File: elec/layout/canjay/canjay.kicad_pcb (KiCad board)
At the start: 6 copper layers, 122 x 100 mm, 150 parts, among them U12 10µH ±20%, U18 10kΩ ±1% 62.5mW, U19 10kΩ ±1% 62.5mW, U20 1µF ±10% 25V X5R, U22 1µF ±10% 25V X5R, U23 10kΩ ±1% 62.5mW, U24 10kΩ ±1% 62.5mW, U25 1µF ±10% 25V X5R, U27 1µF ±10% 25V X5R

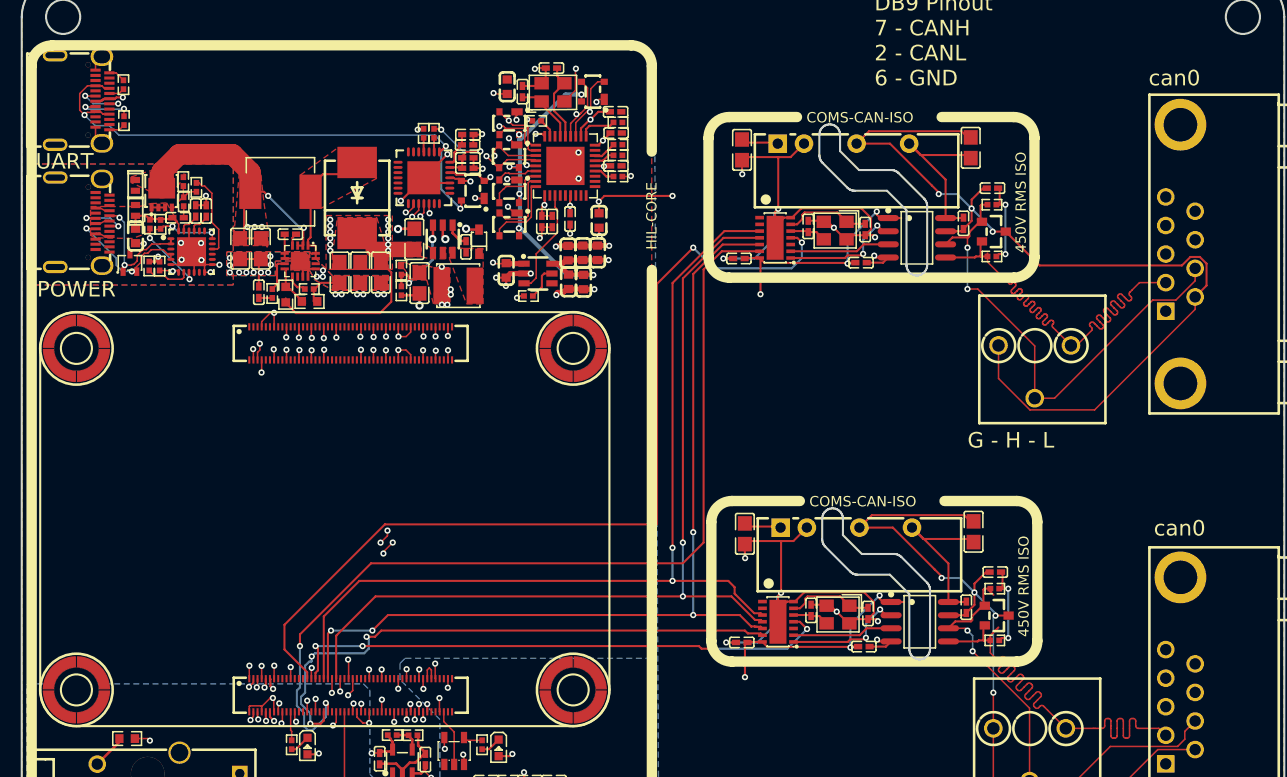
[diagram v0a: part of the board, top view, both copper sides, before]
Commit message: Fix board shapes and CAN termination
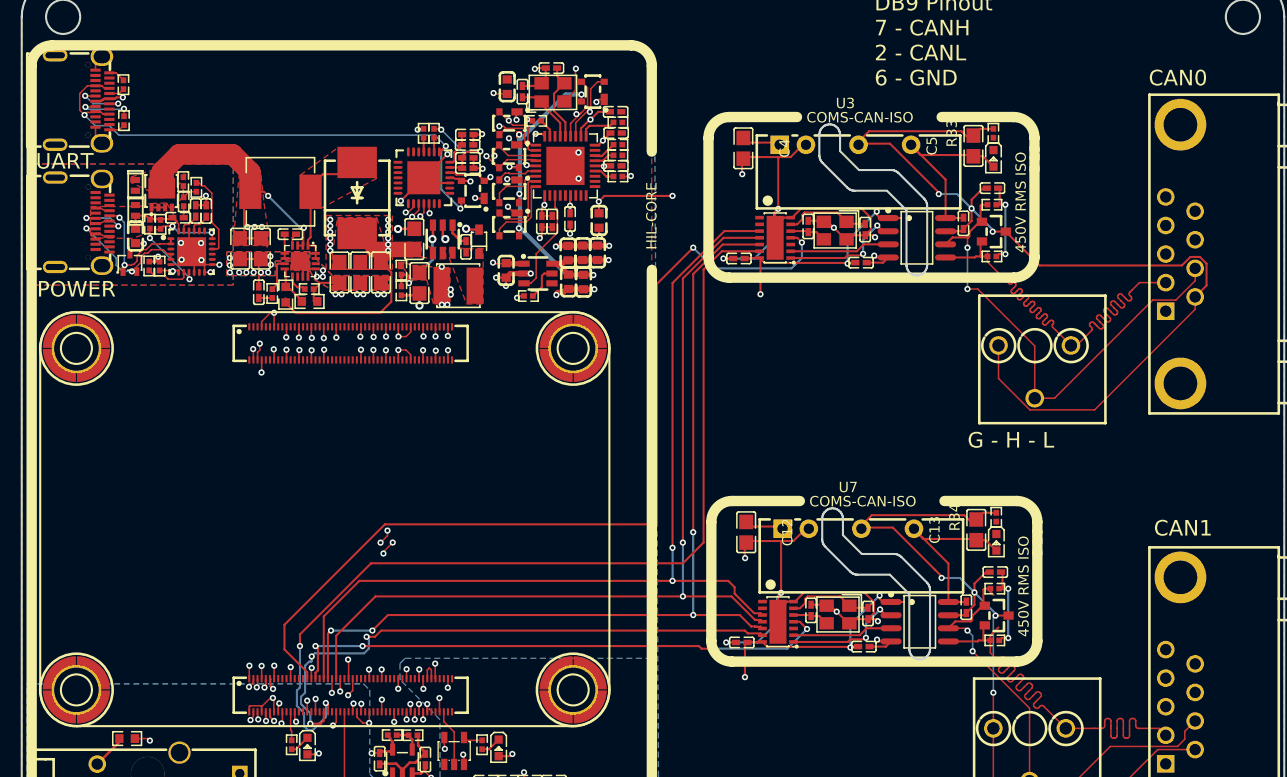
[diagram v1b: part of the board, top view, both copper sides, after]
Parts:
- added D15: , atopile:LED0603-RD-c81ffb, F.Cu at (190.0, 66.4)
- added D16: , atopile:LED0603-RD-c81ffb, F.Cu at (190.3, 103.5)
- added R33: 1kΩ ±1% 62.5mW, atopile:R0402-56259e, F.Cu at (190.0, 64.0)
- added R34: 1kΩ ±1% 62.5mW, atopile:R0402-56259e, F.Cu at (190.3, 101.0)
- C12, C4: value 4.7µF ±10% 25V X5R -> 2.2µF ±10% 25V X7R
- C23, C30, C53: value 4.7µF ±20% 6.3V X5R -> 4.7µF ±20% 10V X5R
- R15: value 560kΩ ±1% 62.5mW -> 510kΩ ±1% 62.5mW
- U14, U15, U16, U17: footprint atopile:SMD_BD5.6-D4.1-12eb58 -> lib:SMD_BD5.6-D4.1-12eb58
- U19: value 10kΩ ±1% 62.5mW -> 18kΩ ±1% 62.5mW
- U24: value 10kΩ ±1% 62.5mW -> 24.9kΩ ±1% 62.5mW
- moved C13 0.32 mm to (188.3, 102.3)
- moved C5 0.32 mm to (188.1, 65.2)
- moved U3 0.22 mm to (175.7, 65.1)
- moved U7 0.22 mm to (176.0, 102.2)
- moved C12 0.20 mm to (166.1, 102.5)
- moved C4 0.20 mm to (165.8, 65.4)
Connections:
- net A6 renamed DP2
- net A7 renamed DN2
- net B5 renamed CC2
- net CC1 renamed A5
- net MDI0plus renamed hil_core.controller-pins[11]
- net MDI2_ renamed hil_core.controller-pins[8]
- net MDI2plus renamed hil_core.controller-pins[10]
- net hil_core.controller-pins[9] renamed MDI0_
- net hil_core.controller.cm5-pins[89] renamed hil_core.controller.cm5-pins[87]-1
- net hil_core.controller.cm5-pins[89]-1 renamed pins[89]
- net hil_core.controller.cm5.hdi_b-pins[9] renamed pins[9]
- net hil_core.ldo_3v3-out renamed hil_core.ldo_3v3-ADJ_NC
- net hil_core.oled.regulator_4v-out renamed hil_core.oled.regulator_4v-ADJ_NC
- net pins[10] renamed hil_core.controller.cm5.hdi_b-pins[10]
- net pins[11] renamed hil_core.controller.cm5.hdi_b-pins[11]
- net pins[87] renamed hil_core.controller.cm5-pins[87]
- net pins[8] renamed hil_core.controller.cm5.hdi_b-pins[8]
- C10 pad 1: xin-2 -> xin
- C13 pad 1: hv -> hv-3
- C16 pad 1: hv -> hv-3
- C18 pad 1: hv-1 -> hv-6
- C19 pad 1: hv-1 -> hv-6
- C29 pad 1: hv-3 -> hv-4
- C30 pad 1: hv-3 -> hv-4
- C42 pad 1: xin -> xin-2
- C45 pad 1: hv-5 -> hv
- C46 pad 1: hv-5 -> hv
- C47 pad 1: hv-5 -> hv
- C48 pad 1: hv-5 -> hv
- C49 pad 1: hv-5 -> hv
- C5 pad 1: hv-2 -> hv-5
- C50 pad 1: hv-4 -> hv-1
- C51 pad 1: hv-4 -> hv-1
- C52 pad 1: hv-6 -> hv-7
- C53 pad 1: hv-6 -> hv-7
- C8 pad 1: hv-2 -> hv-5
- CN1 pad 1: CANL-1 -> CANL
- CN1 pad 2: CANH-1 -> CANH
- CN2 pad 1: CANL -> CANL-1
- CN2 pad 2: CANH -> CANH-1
- CN3 pad 25: hil_core-line-3 -> hil_core-line-6
- CN3 pad 73: hil_core-line-7 -> hil_core-line-8
- CN3 pad 75: hil_core-line -> hil_core-line-5
- CN3 pad 77: hil_core-line-4 -> hil_core-line-10
- CN3 pad 81: line-1 -> line
- CN3 pad 82: line -> line-1
- CN3 pad 86: hil_core-line-5 -> hil_core-line-9
- CN4 pad 98: hil_core-line-8 -> hil_core-line-1
- CN4 pad 99: hil_core-line-10 -> hil_core-line-4
- D1 pad 1: CANH-1 -> CANH
- D1 pad 2: CANL-1 -> CANL
- D10 pad 2: hil_core-line-6 -> hil_core-line-7
- D10 pad 3: hil_core-line-11 -> hil_core-line
- D10 pad 4: hv-5 -> hv
- D11 pad 2: hil_core-line-1 -> hil_core-line-3
- D11 pad 3: hil_core-line-9 -> hil_core-line-11
- D12 pad 1: hil_core.usbpd-line-3 -> hil_core.usbpd-line-2
- D12 pad 2: hil_core.usbpd-line-1 -> hil_core.usbpd-line-3
- D14 pad 1: hv-1 -> hv-6
- D2 pad 1: CANH -> CANH-1
- D2 pad 2: CANL -> CANL-1
- D4 pad 1: hil_core.controller.cm5-cathode-1 -> hil_core.controller.cm5-cathode
- D5 pad 1: hil_core.controller.cm5-cathode -> hil_core.controller.cm5-cathode-1
- D6 pad 2: hil_core-line-1 -> hil_core-line-3
- D6 pad 3: hil_core-line-9 -> hil_core-line-11
- D6 pad 4: hv-5 -> hv
- D7 pad 2: hil_core-line-10 -> hil_core-line-4
- D7 pad 3: hil_core-line-8 -> hil_core-line-1
- D7 pad 4: hv-5 -> hv
- D8 pad 4: hv-5 -> hv
- D9 pad 2: hil_core.usb_hub-line-3 -> hil_core.usb_hub-line
- D9 pad 3: hil_core.usb_hub-line -> hil_core.usb_hub-line-3
- D9 pad 4: hv-5 -> hv
- DSub1 pad 1: can0_db9-net-1 -> can0_db9-net-5
- DSub1 pad 2: CANL-1 -> CANL
- DSub1 pad 3: can0_db9-net -> can0_db9-net-4
- DSub1 pad 4: can0_db9-net-5 -> can0_db9-net
- DSub1 pad 5: can0_db9-net-3 -> can0_db9-net-1
- DSub1 pad 7: CANH-1 -> CANH
- DSub1 pad 8: can0_db9-net-2 -> can0_db9-net-3
- DSub1 pad 9: can0_db9-net-4 -> can0_db9-net-2
- DSub2 pad 1: can1_db9-net-5 -> can1_db9-net-1
- DSub2 pad 2: CANL -> CANL-1
- DSub2 pad 3: can1_db9-net-4 -> can1_db9-net-5
- DSub2 pad 4: can1_db9-net-2 -> can1_db9-net-3
- DSub2 pad 7: CANH -> CANH-1
- DSub2 pad 8: can1_db9-net-1 -> can1_db9-net-4
- DSub2 pad 9: can1_db9-net-3 -> can1_db9-net-2
- L1 pad 1: hv-1 -> hv-6
- OLED1 pad 10: hil_core-line-4 -> hil_core-line-10
- OLED1 pad 14: hv-3 -> hv-4
- OLED1 pad 5: hv-7 -> hv-2
- Q1 pad 5: hv-1 -> hv-6
- Q1 pad 6: hv-1 -> hv-6
- Q1 pad 7: hv-1 -> hv-6
- Q1 pad 8: hv-1 -> hv-6
- Q1 pad 9: hv-1 -> hv-6
- R1 pad 1: CANH-1 -> CANH
- R11 pad 1: hil_core.controller.cm5-cathode-1 -> hil_core.controller.cm5-cathode
- R12 pad 1: hil_core.controller.cm5-cathode -> hil_core.controller.cm5-cathode-1
- R2 pad 2: CANL-1 -> CANL
- R25 pad 2: hv-6 -> hv-7
- R27 pad 1: hil_core.usbpd-line-2 -> hil_core.usbpd-line-1
- R3 pad 1: CANH -> CANH-1
- R30 pad 2: hv-1 -> hv-6
- R4 pad 2: CANL -> CANL-1
- RJ1 pad P1: hil_core.controller.rj45.connector-net -> hil_core.controller.rj45.connector-net-1
- RJ1 pad P10: hil_core.controller.rj45.connector-net-1 -> hil_core.controller.rj45.connector-net
- U1 pad 13: line-1 -> line
- U14 pad 1: hil_core.controller.stud1-net -> GND
- U14 pad 2: hil_core.controller.stud1.footprint.pins[1].net-net -> GND
- U14 pad 3: hil_core.controller.stud1.footprint.pins[2].net-net -> GND
- U14 pad 4: hil_core.controller.stud1.footprint.pins[3].net-net -> GND
- U15 pad 1: hil_core.controller.stud2-net -> GND
- U15 pad 2: hil_core.controller.stud2.footprint.pins[1].net-net -> GND
- U15 pad 3: hil_core.controller.stud2.footprint.pins[2].net-net -> GND
- U15 pad 4: hil_core.controller.stud2.footprint.pins[3].net-net -> GND
- U16 pad 1: hil_core.controller.stud3-net -> GND
- U16 pad 2: hil_core.controller.stud3.footprint.pins[1].net-net -> GND
- U16 pad 3: hil_core.controller.stud3.footprint.pins[2].net-net -> GND
- U16 pad 4: hil_core.controller.stud3.footprint.pins[3].net-net -> GND
- U17 pad 1: hil_core.controller.stud4-net -> GND
- U17 pad 2: hil_core.controller.stud4.footprint.pins[1].net-net -> GND
- U17 pad 3: hil_core.controller.stud4.footprint.pins[2].net-net -> GND
- U17 pad 4: hil_core.controller.stud4.footprint.pins[3].net-net -> GND
- U24 pad 1: hv-7 -> hv-2
- U26 pad 5: hv-7 -> hv-2
- U27 pad 1: hv-7 -> hv-2
- U28 pad 1: hil_core-line-1 -> hil_core-line-3
- U28 pad 2: hil_core-line-9 -> hil_core-line-11
- U28 pad 3: hil_core-line-10 -> hil_core-line-4
- U28 pad 30: hil_core-line-6 -> hil_core-line-7
- U28 pad 31: hil_core-line-11 -> hil_core-line
- U28 pad 33: xin -> xin-2
- U28 pad 4: hil_core-line-8 -> hil_core-line-1
- U28 pad 8: hil_core.usb_hub-line-3 -> hil_core.usb_hub-line
- U28 pad 9: hil_core.usb_hub-line -> hil_core.usb_hub-line-3
- U29 pad 6: hv-5 -> hv
- U3 pad 6: hv-2 -> hv-5
- U30 pad 23: hil_core-line-3 -> hil_core-line-6
- U30 pad 24: hil_core-line-5 -> hil_core-line-9
- U30 pad 25: hil_core-line-7 -> hil_core-line-8
- U30 pad 26: hil_core-line -> hil_core-line-5
- U30 pad 4: hil_core-line-9 -> hil_core-line-11
- U30 pad 5: hil_core-line-1 -> hil_core-line-3
- U30 pad 6: hv-6 -> hv-7
- U30 pad 7: hv-4 -> hv-1
- U31 pad 1: hil_core.usbpd-line-3 -> hil_core.usbpd-line-2
- U31 pad 2: hil_core.usbpd-line-3 -> hil_core.usbpd-line-2
- U31 pad 4: hil_core.usbpd-line-1 -> hil_core.usbpd-line-3
- U31 pad 5: hil_core.usbpd-line-1 -> hil_core.usbpd-line-3
- U31 pad 7: hil_core.usbpd-line-2 -> hil_core.usbpd-line-1
- U32 pad 1: _boardshape.handle-net-1 -> _boardshape.handle-net
- U32 pad 2: _boardshape.handle-net -> _boardshape.handle-net-1
- U4 pad 5: CANL-1 -> CANL
- U4 pad 6: CANH-1 -> CANH
- U4 pad 8: hv-2 -> hv-5
- U5 pad 13: line -> line-1
- U5 pad 6: xin-2 -> xin
- U6 pad 1: xin-2 -> xin
- U7 pad 6: hv -> hv-3
- U8 pad 5: CANL -> CANL-1
- U8 pad 6: CANH -> CANH-1
- U8 pad 8: hv -> hv-3
- U9 pad 2: hv-1 -> hv-6
- U9 pad 3: hv-1 -> hv-6
- USB1 pad A6: hil_core-line-11 -> hil_core-line
- USB1 pad A7: hil_core-line-6 -> hil_core-line-7
- USB1 pad B6: hil_core-line-11 -> hil_core-line
- USB1 pad B7: hil_core-line-6 -> hil_core-line-7
- USB2 pad A5: hil_core.usbpd-line-3 -> hil_core.usbpd-line-2
- USB2 pad B5: hil_core.usbpd-line-1 -> hil_core.usbpd-line-3
- X1 pad 1: xin -> xin-2
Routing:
- net hil_core-line-9: track 15.5 -> 55.0 mm
- net hil_core-line-11: track 54.2 -> 15.5 mm
- net line-1: track 89.5 -> 55.5 mm, vias 2 -> 3
- net line: track 55.5 -> 89.5 mm, vias 3 -> 2
- net hil_core-line-3: track 49.5 -> 16.5 mm, vias 4 -> 2
- net hv-1: track 30.5 -> 3.36 mm, vias 5 -> 0
- net hv: track 16.7 -> 41.6 mm, vias 0 -> 7
- net hv-5: track 41.6 -> 19.0 mm, vias 7 -> 0
- net hil_core-line-1: track 16.5 -> 38.1 mm
- net hv-6: track 10.7 -> 30.5 mm, vias 2 -> 5
- net hv-3: track 4.40 -> 19.0 mm, vias 1 -> 0
- net hil_core-line-8: track 38.1 -> 52.1 mm, vias 2 -> 4
- net hil_core-line-4: track 26.6 -> 38.7 mm, vias 1 -> 2
- net hil_core-line-10: track 38.7 -> 26.6 mm, vias 2 -> 1
- net hil_core.usbpd-line-1: track 13.0 -> 2.17 mm, vias 2 -> 1
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- added copper zone on F.Cu, net hv-6
- removed copper zone on F.Cu, net hv-1
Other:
- board text added: "CAN0"
- board text added: "CAN1"
- board text removed: "can0"

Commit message: drc fixes
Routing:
- net can0.regulator.led-cathode: track 0.00 -> 1.19 mm
- net can1.regulator.led-cathode: track 0.00 -> 1.19 mm
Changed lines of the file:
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@@
 			(remove_unused_layers yes)
 			(keep_end_layers yes)
-			(zone_layer_connections)
+			(zone_layer_connections "In2.Cu")
 			(net 157 "GND")
 		)
@@
 			(remove_unused_layers yes)
 			(keep_end_layers yes)
-			(zone_layer_connections)
+			(zone_layer_connections "In2.Cu")
 			(net 157 "GND")
 		)
@@
 			(remove_unused_layers yes)
 			(keep_end_layers yes)
-			(zone_layer_connections)
+			(zone_layer_connections "In2.Cu")
 			(net 157 "GND")
 		)
@@
 			(remove_unused_layers yes)
 			(keep_end_layers yes)
-			(zone_layer_connections)
+			(zone_layer_connections "In2.Cu")
 			(net 157 "GND")
 		)
@@
 	)
 	(segment
+		(start 190.28 101.48)
+		(end 190.28 102.66)
+		(width 0.15)
+		(layer "F.Cu")
+		(net 311)
+	)
+	(segment
+		(start 190.28 102.66)
+		(end 190.29 102.67)
+		(width 0.15)
+		(layer "F.Cu")
+		(net 311)
+	)
+	(segment
 		(start 182.965 66.05)
 		(end 181.865 64.95)
@@
 	)
 	(segment
+		(start 190.005 64.38)
+		(end 190.005 65.56)
+		(width 0.15)
+		(layer "F.Cu")
+		(net 314)
+	)
+	(segment
+		(start 190.005 65.56)
+		(end 190.015 65.57)
+		(width 0.15)
+		(layer "F.Cu")
+		(net 314)
+	)
+	(segment
 		(start 185.093543 73.42)
 		(end 185.385 73.42)
@@
 		(connect_pads yes
 			(clearance 0)
+		)
+		(min_thickness 0.0254)
+		(filled_areas_thickness no)
+		(fill yes
+			(thermal_gap 0.5)
+			(thermal_bridge_width 0.5)
+			(island_removal_mode 1)
+			(island_area_min 10)
+		)
+		(polygon
+			(pts
+				(xy 136.625011 77.438767) (xy 136.775011 77.438767) (xy 136.994247 76.903058) (xy 136.700011 76.843531)
+				(xy 136.405775 76.903058)
+			)
+		)
+	)
+	(zone
+		(net 261)
+		(net_name "POWER_5V")
+		(layer "F.Cu")
+		(name "$teardrop_padvia$")
+		(hatch full 0.1)
+		(priority 30000)
+		(attr
+			(teardrop
+				(type padvia)
+			)
+		)
+		(connect_pads yes
+			(clearance 0)

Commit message: Build everything with ordered params to fix frozen builds
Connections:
- net A10 renamed hil_core.usbpd.usb_connector-A10
- net A11 renamed hil_core.usbpd.usb_connector-A11
- net A5 renamed CC1
- net B2 renamed hil_core.usbpd.usb_connector-B2
- net B3 renamed hil_core.usbpd.usb_connector-B3
- net B8 renamed hil_core.usbpd.usb_connector-B8
- net CC2 renamed B5
- net DN2 renamed DN1
- net DP2 renamed DP1
- net MDI0_ renamed hil_core.controller-pins[9]
- net MDI1plus renamed hil_core.controller-pins[3]
- net SBU2 renamed hil_core.usb_connector.connector-B8
- net SSRXN2 renamed hil_core.usb_connector.connector-A10
- net SSRXP2 renamed hil_core.usb_connector.connector-A11
- net SSTXN2 renamed hil_core.usb_connector.connector-B3
- net SSTXP2 renamed hil_core.usb_connector.connector-B2
- net hil_core.controller-pins[10] renamed MDI2plus
- net hil_core.controller-pins[11] renamed MDI0plus
- net hil_core.controller-pins[8] renamed MDI2_
- net hil_core.controller.cm5-pins[87] renamed pins[87]
- net hil_core.controller.cm5-pins[87]-1 renamed hil_core.controller.cm5-pins[89]
- net hil_core.controller.cm5.hdi_b-pins[10] renamed pins[10]
- net hil_core.controller.cm5.hdi_b-pins[11] renamed pins[11]
- net hil_core.controller.cm5.hdi_b-pins[8] renamed pins[8]
- net hil_core.usb_connector.connector-A2 renamed hil_core.usb_connector.connector-SSTXP1
- net hil_core.usb_connector.connector-A3 renamed SSTXN1
- net hil_core.usb_connector.connector-A8 renamed SBU1
- net hil_core.usb_connector.connector-B10 renamed SSRXN1
- net hil_core.usb_connector.connector-B11 renamed SSRXP1
- net hil_core.usbpd.usb_connector-A2 renamed hil_core.usbpd.usb_connector-SSTXP1
- net hil_core.usbpd.usb_connector-A3 renamed A3
- net hil_core.usbpd.usb_connector-A8 renamed A8
- net hil_core.usbpd.usb_connector-B10 renamed B10
- net hil_core.usbpd.usb_connector-B11 renamed B11
- net pins[3] renamed hil_core.controller.cm5.hdi_b-pins[3]
- net pins[4] renamed MDI3_
- net pins[89] renamed hil_core.controller.cm5-pins[89]-1
- net pins[9] renamed hil_core.controller.cm5.hdi_b-pins[9]
- C10 pad 1: xin -> xin-2
- C13 pad 1: hv-3 -> hv-4
- C13 pad 2: gnd-1 -> gnd
- C14 pad 2: gnd-1 -> gnd
- C16 pad 1: hv-3 -> hv-4
- C16 pad 2: gnd-1 -> gnd
- C29 pad 1: hv-4 -> hv
- C3 pad 1: xout-1 -> xout
- C30 pad 1: hv-4 -> hv
- C42 pad 1: xin-2 -> xin
- C43 pad 1: xout -> xout-1
- C45 pad 1: hv -> hv-3
- C46 pad 1: hv -> hv-3
- C47 pad 1: hv -> hv-3
- C48 pad 1: hv -> hv-3
- C49 pad 1: hv -> hv-3
- C5 pad 2: gnd -> gnd-1
- C55 pad 2: hil_core.usbpd.pd_controller-hv-1 -> hil_core.usbpd.pd_controller-hv
- C56 pad 2: hil_core.usbpd.pd_controller-hv -> hil_core.usbpd.pd_controller-hv-1
- C6 pad 2: gnd -> gnd-1
- C8 pad 2: gnd -> gnd-1
- CN1 pad 1: CANL -> CANL-1
- CN1 pad 3: gnd -> gnd-1
- CN2 pad 1: CANL-1 -> CANL
- CN2 pad 3: gnd-1 -> gnd
- CN3 pad 23: hil_core-line-2 -> hil_core-line-1
- CN3 pad 24: hil_core.controller.cm5-pins[47] -> hil_core.controller.cm5-pins[47]-1
- CN3 pad 25: hil_core-line-6 -> hil_core-line-8
- CN3 pad 27: hil_core.controller.cm5-pins[53]-1 -> hil_core.controller.cm5-pins[53]
- CN3 pad 73: hil_core-line-8 -> hil_core-line-11
- CN3 pad 75: hil_core-line-5 -> hil_core-line-9
- CN3 pad 76: hil_core.controller.cm5-pins[48]-1 -> hil_core.controller.cm5-pins[48]
- CN3 pad 77: hil_core-line-10 -> hil_core-line-3
- CN3 pad 81: line -> line-1
- CN3 pad 82: line-1 -> line
- CN3 pad 86: hil_core-line-9 -> hil_core-line-5
- CN4 pad 24: hil_core.controller.cm5-pins[47]-1 -> hil_core.controller.cm5-pins[47]
- CN4 pad 27: hil_core.controller.cm5-pins[53] -> hil_core.controller.cm5-pins[53]-1
- CN4 pad 76: hil_core.controller.cm5-pins[48] -> hil_core.controller.cm5-pins[48]-1
- CN4 pad 98: hil_core-line-1 -> hil_core-line-2
- CN4 pad 99: hil_core-line-4 -> hil_core-line-10
- D1 pad 2: CANL -> CANL-1
- D1 pad 3: gnd -> gnd-1
- D10 pad 2: hil_core-line-7 -> hil_core-line-6
- D10 pad 3: hil_core-line -> hil_core-line-7
- D10 pad 4: hv -> hv-3
- D11 pad 2: hil_core-line-3 -> hil_core-line-4
- D11 pad 3: hil_core-line-11 -> hil_core-line
- D12 pad 1: hil_core.usbpd-line-2 -> hil_core.usbpd-line-3
- D12 pad 2: hil_core.usbpd-line-3 -> hil_core.usbpd-line-1
- D16 pad 2: hv-3 -> hv-4
- D2 pad 2: CANL-1 -> CANL
- D2 pad 3: gnd-1 -> gnd
- D6 pad 2: hil_core-line-3 -> hil_core-line-4
- D6 pad 3: hil_core-line-11 -> hil_core-line
- D6 pad 4: hv -> hv-3
- D7 pad 2: hil_core-line-4 -> hil_core-line-10
- D7 pad 3: hil_core-line-1 -> hil_core-line-2
- D7 pad 4: hv -> hv-3
- D8 pad 2: hil_core.usb_hub-line-1 -> hil_core.usb_hub-line-3
- D8 pad 3: hil_core.usb_hub-line-2 -> hil_core.usb_hub-line-1
- D8 pad 4: hv -> hv-3
- D9 pad 3: hil_core.usb_hub-line-3 -> hil_core.usb_hub-line-2
- D9 pad 4: hv -> hv-3
- DSub1 pad 1: can0_db9-net-5 -> can0_db9-net-1
- DSub1 pad 2: CANL -> CANL-1
- DSub1 pad 3: can0_db9-net-4 -> can0_db9-net
- DSub1 pad 4: can0_db9-net -> can0_db9-net-5
- DSub1 pad 5: can0_db9-net-1 -> can0_db9-net-4
- DSub1 pad 6: gnd -> gnd-1
- DSub1 pad 8: can0_db9-net-3 -> can0_db9-net-2
- DSub1 pad 9: can0_db9-net-2 -> can0_db9-net-3
- DSub2 pad 1: can1_db9-net-1 -> can1_db9-net
- DSub2 pad 2: CANL-1 -> CANL
- DSub2 pad 3: can1_db9-net-5 -> can1_db9-net-4
- DSub2 pad 4: can1_db9-net-3 -> can1_db9-net-2
- DSub2 pad 5: can1_db9-net -> can1_db9-net-3
- DSub2 pad 6: gnd-1 -> gnd
- DSub2 pad 8: can1_db9-net-4 -> can1_db9-net-1
- DSub2 pad 9: can1_db9-net-2 -> can1_db9-net-5
- OLED1 pad 10: hil_core-line-10 -> hil_core-line-3
- OLED1 pad 11: hil_core-line-2 -> hil_core-line-1
- OLED1 pad 14: hv-4 -> hv
- R2 pad 2: CANL -> CANL-1
- R27 pad 1: hil_core.usbpd-line-1 -> hil_core.usbpd-line-2
- R33 pad 2: gnd -> gnd-1
- R34 pad 2: gnd-1 -> gnd
- R4 pad 2: CANL-1 -> CANL
- U1 pad 13: line -> line-1
- U1 pad 5: xout-1 -> xout
- U2 pad 3: xout-1 -> xout
- U28 pad 1: hil_core-line-3 -> hil_core-line-4
- U28 pad 2: hil_core-line-11 -> hil_core-line
- U28 pad 3: hil_core-line-4 -> hil_core-line-10
- U28 pad 30: hil_core-line-7 -> hil_core-line-6
- U28 pad 31: hil_core-line -> hil_core-line-7
- U28 pad 32: xout -> xout-1
- U28 pad 33: xin-2 -> xin
- U28 pad 4: hil_core-line-1 -> hil_core-line-2
- U28 pad 6: hil_core.usb_hub-line-1 -> hil_core.usb_hub-line-3
- U28 pad 7: hil_core.usb_hub-line-2 -> hil_core.usb_hub-line-1
- U28 pad 9: hil_core.usb_hub-line-3 -> hil_core.usb_hub-line-2
- U29 pad 6: hv -> hv-3
- U3 pad 4: gnd -> gnd-1
- U30 pad 23: hil_core-line-6 -> hil_core-line-8
- U30 pad 24: hil_core-line-9 -> hil_core-line-5
- U30 pad 25: hil_core-line-8 -> hil_core-line-11
- U30 pad 26: hil_core-line-5 -> hil_core-line-9
- U30 pad 4: hil_core-line-11 -> hil_core-line
- U30 pad 5: hil_core-line-3 -> hil_core-line-4
- U31 pad 1: hil_core.usbpd-line-2 -> hil_core.usbpd-line-3
- U31 pad 2: hil_core.usbpd-line-2 -> hil_core.usbpd-line-3
- U31 pad 21: hil_core.usbpd.pd_controller-hv-1 -> hil_core.usbpd.pd_controller-hv
- U31 pad 23: hil_core.usbpd.pd_controller-hv -> hil_core.usbpd.pd_controller-hv-1
- U31 pad 4: hil_core.usbpd-line-3 -> hil_core.usbpd-line-1
- U31 pad 5: hil_core.usbpd-line-3 -> hil_core.usbpd-line-1
- U31 pad 7: hil_core.usbpd-line-1 -> hil_core.usbpd-line-2
- U32 pad 1: _boardshape.handle-net -> _boardshape.handle-net-1
- U32 pad 2: _boardshape.handle-net-1 -> _boardshape.handle-net
- U4 pad 5: CANL -> CANL-1
- U4 pad 7: gnd -> gnd-1
- U5 pad 13: line-1 -> line
- U5 pad 6: xin -> xin-2
- U6 pad 1: xin -> xin-2
- U7 pad 4: gnd-1 -> gnd
- U7 pad 6: hv-3 -> hv-4
- U8 pad 5: CANL-1 -> CANL
- U8 pad 7: gnd-1 -> gnd
- U8 pad 8: hv-3 -> hv-4
- USB1 pad A6: hil_core-line -> hil_core-line-7
- USB1 pad A7: hil_core-line-7 -> hil_core-line-6
- USB1 pad B6: hil_core-line -> hil_core-line-7
- USB1 pad B7: hil_core-line-7 -> hil_core-line-6
- USB2 pad A5: hil_core.usbpd-line-2 -> hil_core.usbpd-line-3
- USB2 pad B5: hil_core.usbpd-line-3 -> hil_core.usbpd-line-1
- X1 pad 1: xin-2 -> xin
- X1 pad 3: xout -> xout-1
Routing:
- net hil_core-line: track 54.2 -> 15.5 mm
- net hv: track 41.6 -> 4.40 mm, vias 7 -> 1
- net hil_core-line-11: track 15.5 -> 52.1 mm, vias 2 -> 4
- net line-1: track 55.5 -> 89.5 mm, vias 3 -> 2
- net line: track 89.5 -> 55.5 mm, vias 2 -> 3
- net hv-3: track 19.0 -> 41.6 mm, vias 0 -> 7
- net hil_core-line-4: track 38.7 -> 16.5 mm
- net hv-4: track 4.40 -> 19.0 mm, vias 1 -> 0
- net gnd-1: track 82.0 -> 94.6 mm, vias 4 -> 3
- net gnd: track 94.6 -> 82.0 mm, vias 3 -> 4
- net hil_core-line-10: track 26.6 -> 38.7 mm, vias 1 -> 2
- net hil_core.usbpd-line-1: track 2.17 -> 13.0 mm, vias 1 -> 2
- net hil_core.usbpd-line-2: track 12.9 -> 2.17 mm, vias 2 -> 1
- net hil_core-line-3: track 16.5 -> 26.6 mm, vias 2 -> 1
- net hil_core-line-6: track 49.5 -> 59.1 mm, vias 4 -> 3
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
